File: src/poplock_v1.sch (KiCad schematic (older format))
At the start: 0 parts

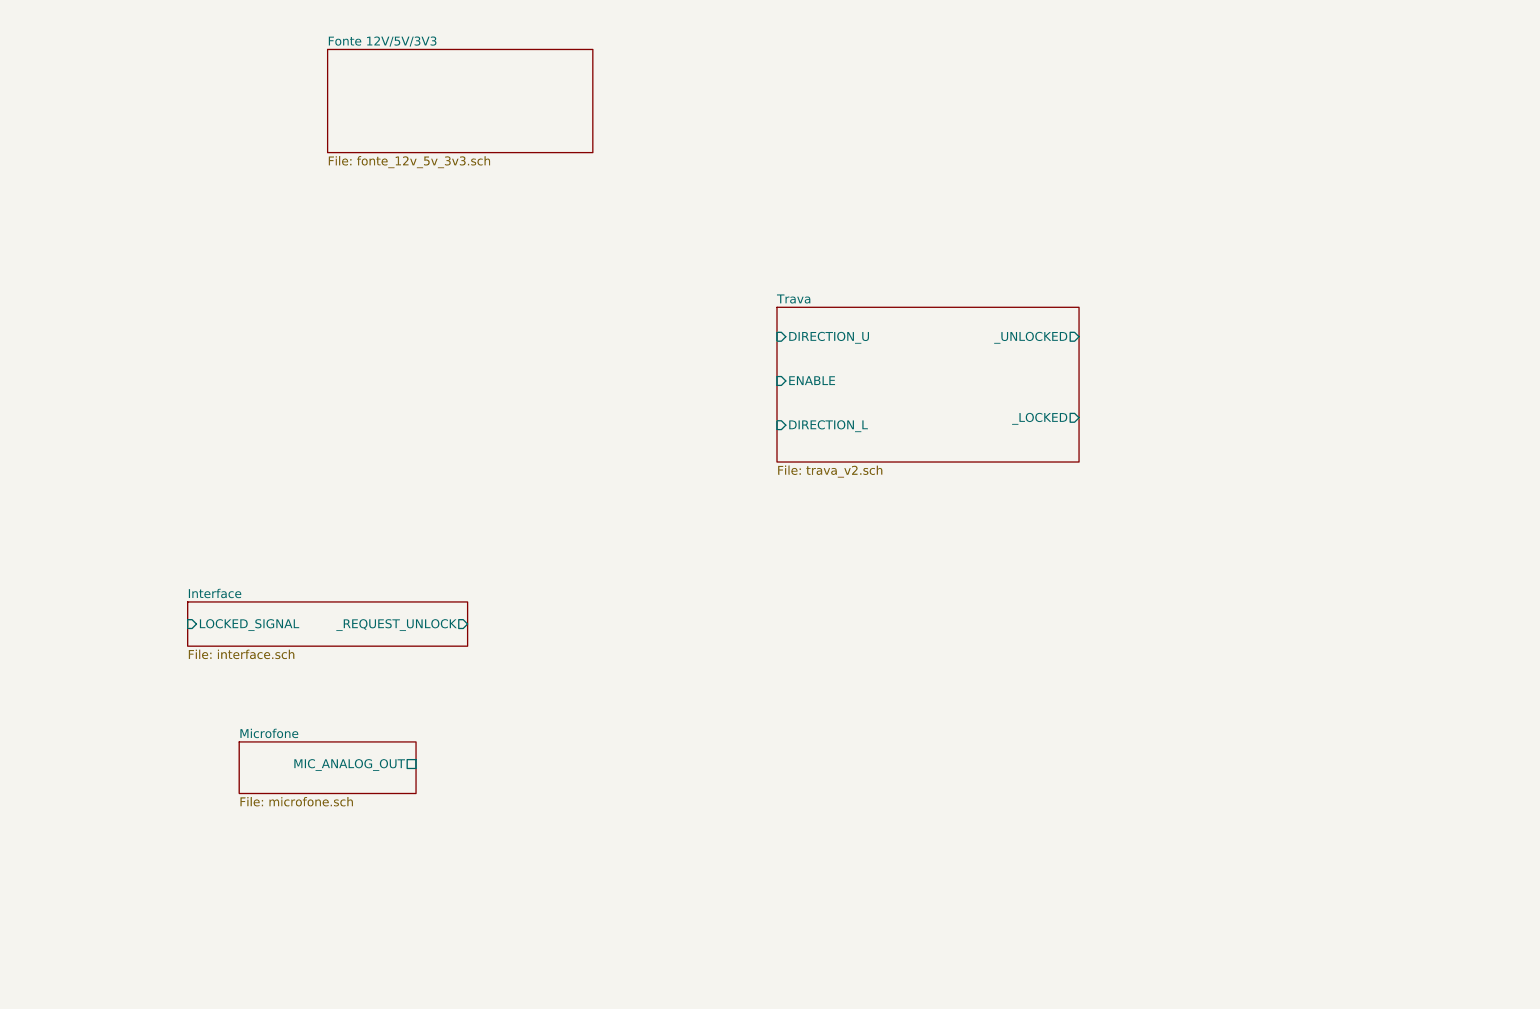
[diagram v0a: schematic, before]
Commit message: Adicionados conectores da FRDM-KL25Z e conexões básicas de alimentação
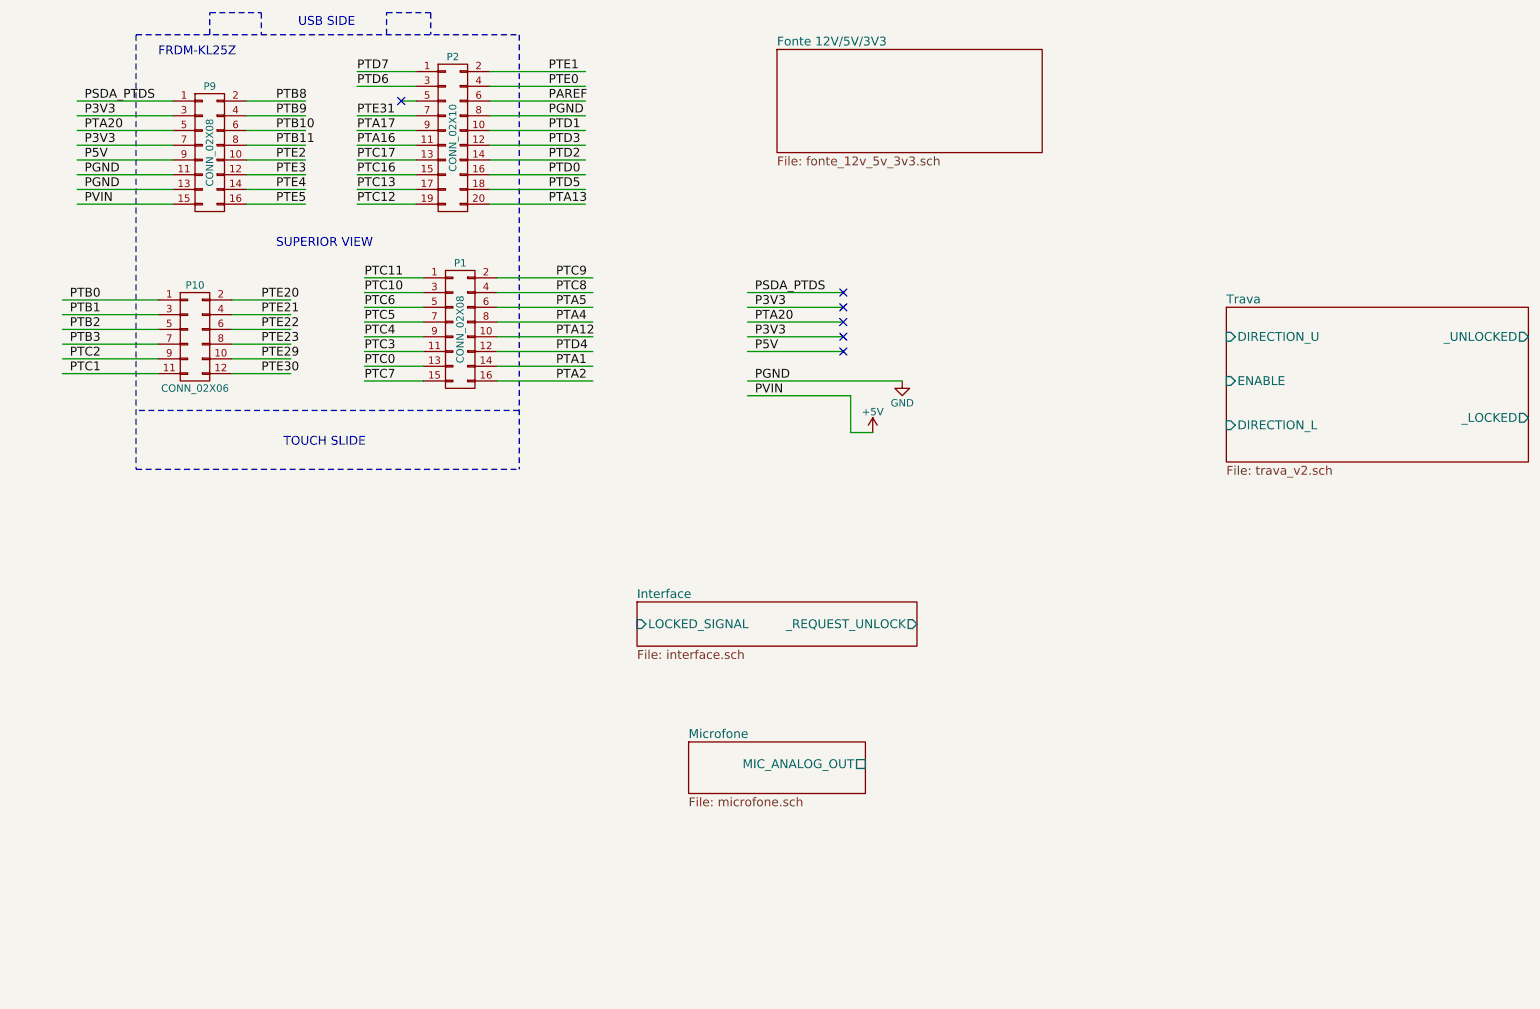
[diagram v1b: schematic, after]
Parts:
- added P1, P9: CONN_02X08, symbol CONN_02X08
- added P10: CONN_02X06, symbol CONN_02X06
- added P2: CONN_02X10, symbol CONN_02X10
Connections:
- net labels added: +5V, GND, P3V3, P5V, PAREF, PGND, PSDA_PTDS, PTA1, PTA12, PTA13, PTA16, PTA17, PTA2, PTA20, PTA4, PTA5, PTB0, PTB1, PTB10, PTB11, PTB2, PTB3, PTB8, PTB9, PTC0, PTC1, PTC10, PTC11, PTC12, PTC13, PTC16, PTC17, PTC2, PTC3, PTC4, PTC5, PTC6, PTC7, PTC8, PTC9, PTD0, PTD1, PTD2, PTD3, PTD4, PTD5, PTD6, PTD7, PTE0, PTE1, PTE2, PTE20, PTE21, PTE22, PTE23, PTE29, PTE3, PTE30, PTE31, PTE4, PTE5, PVIN
- wire segments 0 -> 73
- no-connect marks 0 -> 6
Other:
- note added: "FRDM-KL25Z"
- note added: "SUPERIOR VIEW"
- note added: "TOUCH SLIDE"
- note added: "USB SIDE"

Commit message: Acréscimo de bibliotecas de símbolo e de footprint do ESP12E retiradas de https://github.com/jdunmire/kicad-ESP8266 . As conexões necessárias com a KL25Z também foram realizadas.
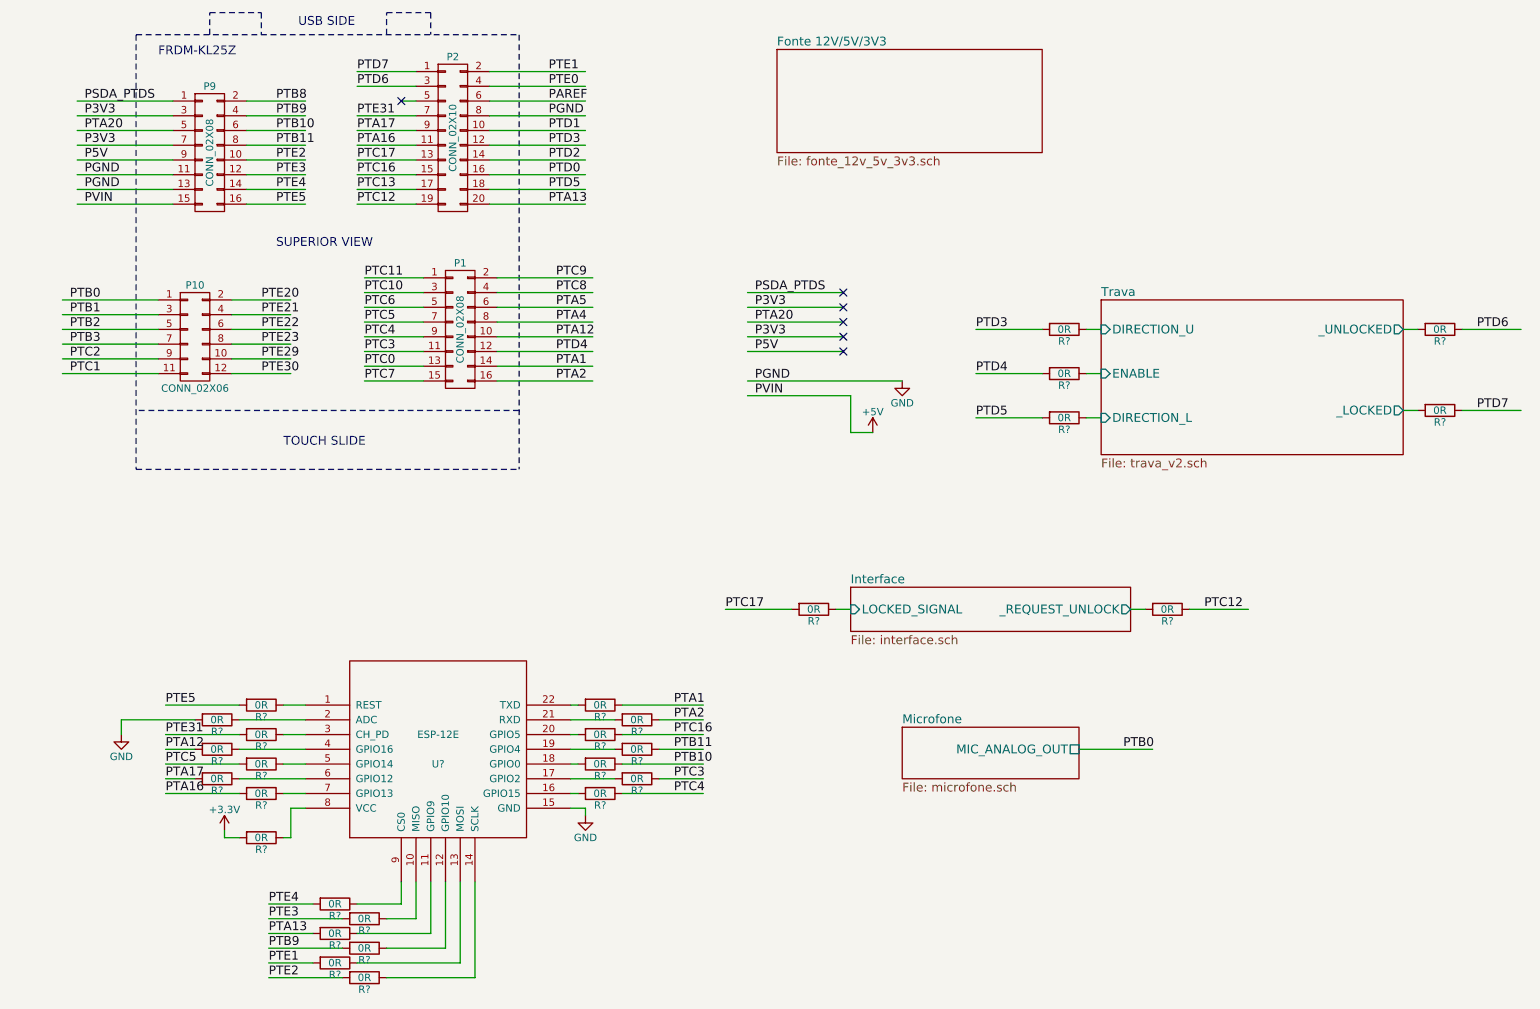
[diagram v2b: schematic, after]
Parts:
- added R? (x28): 0R, symbol R
- added U?: ESP-12E, symbol ESP-12E
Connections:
- net labels added: +3.3V
- wire segments 73 -> 142

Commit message: Verificação ERC -- checagem de erros elétricos no esquema -- concluída com sucesso. Há apenas dois warnings que não indicam problemas.
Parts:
- P1, P9: footprint (none) -> Pin_Headers:Pin_Header_Straight_2x08
- P10: footprint (none) -> Pin_Headers:Pin_Header_Straight_2x06
- P2: footprint (none) -> Pin_Headers:Pin_Header_Straight_2x10
- R23: renamed from R?; footprint (none) -> SMD_Packages:SMD-1210_Pol
- gave numbers to parts that had none: 28
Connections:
- net labels added: P3V3_2
- wire segments 142 -> 136
- no-connect marks 6 -> 33

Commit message: Footprint atualizado
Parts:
- R1, R10, R11, R12, R13, R14, R15, R16, R17, R18, R19, R2, R20, R21, R22, R24, R25, R26, R27, R28, R3, R4, R5, R6, R7, R8, R9: footprint (none) -> Resistors_SMD:R_0603_HandSoldering
- R23: footprint SMD_Packages:SMD-1210_Pol -> Resistors_SMD:R_0603_HandSoldering
- U1: footprint (none) -> lib:ESP-12E
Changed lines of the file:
@@
 F 0 "U1" H 3500 5450 50  0000 C CNN
 F 1 "ESP-12E" H 3500 5650 50  0000 C CNN
-F 2 "" H 3500 5550 50  0001 C CNN
+F 2 "lib:ESP-12E" H 3500 5550 50  0001 C CNN
 F 3 "" H 3500 5550 50  0001 C CNN
 	1    3500 5550
@@
 F 0 "R4" V 2380 5250 50  0000 C CNN
 F 1 "0R" V 2300 5250 50  0000 C CNN
-F 2 "" V 2230 5250 50  0001 C CNN
+F 2 "Resistors_SMD:R_0603_HandSoldering" V 2230 5250 50  0001 C CNN
 F 3 "" H 2300 5250 50  0000 C CNN
 	1    2300 5250
@@
 F 0 "R1" V 2080 5350 50  0000 C CNN
 F 1 "0R" V 2000 5350 50  0000 C CNN
-F 2 "" V 1930 5350 50  0001 C CNN
+F 2 "Resistors_SMD:R_0603_HandSoldering" V 1930 5350 50  0001 C CNN
 F 3 "" H 2000 5350 50  0000 C CNN
 	1    2000 5350
@@
 F 0 "R5" V 2380 5450 50  0000 C CNN
 F 1 "0R" V 2300 5450 50  0000 C CNN
-F 2 "" V 2230 5450 50  0001 C CNN
+F 2 "Resistors_SMD:R_0603_HandSoldering" V 2230 5450 50  0001 C CNN
 F 3 "" H 2300 5450 50  0000 C CNN
 	1    2300 5450
@@
 F 0 "R2" V 2080 5550 50  0000 C CNN
 F 1 "0R" V 2000 5550 50  0000 C CNN
-F 2 "" V 1930 5550 50  0001 C CNN
+F 2 "Resistors_SMD:R_0603_HandSoldering" V 1930 5550 50  0001 C CNN
 F 3 "" H 2000 5550 50  0000 C CNN
 	1    2000 5550
@@
 F 0 "R6" V 2380 5650 50  0000 C CNN
 F 1 "0R" V 2300 5650 50  0000 C CNN
-F 2 "" V 2230 5650 50  0001 C CNN
+F 2 "Resistors_SMD:R_0603_HandSoldering" V 2230 5650 50  0001 C CNN
 F 3 "" H 2300 5650 50  0000 C CNN
 	1    2300 5650
@@
 F 0 "R3" V 2080 5750 50  0000 C CNN
 F 1 "0R" V 2000 5750 50  0000 C CNN
-F 2 "" V 1930 5750 50  0001 C CNN
+F 2 "Resistors_SMD:R_0603_HandSoldering" V 1930 5750 50  0001 C CNN
 F 3 "" H 2000 5750 50  0000 C CNN
 	1    2000 5750
@@
 F 0 "R7" V 2380 5850 50  0000 C CNN
 F 1 "0R" V 2300 5850 50  0000 C CNN
-F 2 "" V 2230 5850 50  0001 C CNN
+F 2 "Resistors_SMD:R_0603_HandSoldering" V 2230 5850 50  0001 C CNN
 F 3 "" H 2300 5850 50  0000 C CNN
 	1    2300 5850
@@
 F 0 "R8" V 2380 6150 50  0000 C CNN
 F 1 "0R" V 2300 6150 50  0000 C CNN
-F 2 "" V 2230 6150 50  0001 C CNN
+F 2 "Resistors_SMD:R_0603_HandSoldering" V 2230 6150 50  0001 C CNN
 F 3 "" H 2300 6150 50  0000 C CNN
 	1    2300 6150
@@
 F 0 "R18" V 4680 5850 50  0000 C CNN
 F 1 "0R" V 4600 5850 50  0000 C CNN
-F 2 "" V 4530 5850 50  0001 C CNN
+F 2 "Resistors_SMD:R_0603_HandSoldering" V 4530 5850 50  0001 C CNN
 F 3 "" H 4600 5850 50  0000 C CNN
 	1    4600 5850
@@
 F 0 "R21" V 4930 5750 50  0000 C CNN
 F 1 "0R" V 4850 5750 50  0000 C CNN
-F 2 "" V 4780 5750 50  0001 C CNN
+F 2 "Resistors_SMD:R_0603_HandSoldering" V 4780 5750 50  0001 C CNN
 F 3 "" H 4850 5750 50  0000 C CNN
 	1    4850 5750
@@
 F 0 "R17" V 4680 5650 50  0000 C CNN
 F 1 "0R" V 4600 5650 50  0000 C CNN
-F 2 "" V 4530 5650 50  0001 C CNN
+F 2 "Resistors_SMD:R_0603_HandSoldering" V 4530 5650 50  0001 C CNN
 F 3 "" H 4600 5650 50  0000 C CNN
 	1    4600 5650
@@
 F 0 "R20" V 4930 5550 50  0000 C CNN
 F 1 "0R" V 4850 5550 50  0000 C CNN
-F 2 "" V 4780 5550 50  0001 C CNN
+F 2 "Resistors_SMD:R_0603_HandSoldering" V 4780 5550 50  0001 C CNN
 F 3 "" H 4850 5550 50  0000 C CNN
 	1    4850 5550
@@
 F 0 "R16" V 4680 5450 50  0000 C CNN
 F 1 "0R" V 4600 5450 50  0000 C CNN
-F 2 "" V 4530 5450 50  0001 C CNN
+F 2 "Resistors_SMD:R_0603_HandSoldering" V 4530 5450 50  0001 C CNN
 F 3 "" H 4600 5450 50  0000 C CNN
 	1    4600 5450
@@
 F 0 "R19" V 4930 5350 50  0000 C CNN
 F 1 "0R" V 4850 5350 50  0000 C CNN
-F 2 "" V 4780 5350 50  0001 C CNN
+F 2 "Resistors_SMD:R_0603_HandSoldering" V 4780 5350 50  0001 C CNN
 F 3 "" H 4850 5350 50  0000 C CNN
 	1    4850 5350
@@
 F 0 "R15" V 4680 5250 50  0000 C CNN
 F 1 "0R" V 4600 5250 50  0000 C CNN
-F 2 "" V 4530 5250 50  0001 C CNN
+F 2 "Resistors_SMD:R_0603_HandSoldering" V 4530 5250 50  0001 C CNN
 F 3 "" H 4600 5250 50  0000 C CNN
 	1    4600 5250
@@
 F 0 "R9" V 2880 6600 50  0000 C CNN
 F 1 "0R" V 2800 6600 50  0000 C CNN
-F 2 "" V 2730 6600 50  0001 C CNN
+F 2 "Resistors_SMD:R_0603_HandSoldering" V 2730 6600 50  0001 C CNN
 F 3 "" H 2800 6600 50  0000 C CNN
 	1    2800 6600
@@
 F 0 "R12" V 3080 6700 50  0000 C CNN
 F 1 "0R" V 3000 6700 50  0000 C CNN
-F 2 "" V 2930 6700 50  0001 C CNN
+F 2 "Resistors_SMD:R_0603_HandSoldering" V 2930 6700 50  0001 C CNN
 F 3 "" H 3000 6700 50  0000 C CNN
 	1    3000 6700
@@
 F 0 "R10" V 2880 6800 50  0000 C CNN
 F 1 "0R" V 2800 6800 50  0000 C CNN
-F 2 "" V 2730 6800 50  0001 C CNN
+F 2 "Resistors_SMD:R_0603_HandSoldering" V 2730 6800 50  0001 C CNN
 F 3 "" H 2800 6800 50  0000 C CNN
 	1    2800 6800
@@
 F 0 "R13" V 3080 6900 50  0000 C CNN
 F 1 "0R" V 3000 6900 50  0000 C CNN
-F 2 "" V 2930 6900 50  0001 C CNN
+F 2 "Resistors_SMD:R_0603_HandSoldering" V 2930 6900 50  0001 C CNN
 F 3 "" H 3000 6900 50  0000 C CNN
 	1    3000 6900
@@
 F 0 "R11" V 2880 7000 50  0000 C CNN
 F 1 "0R" V 2800 7000 50  0000 C CNN
-F 2 "" V 2730 7000 50  0001 C CNN
+F 2 "Resistors_SMD:R_0603_HandSoldering" V 2730 7000 50  0001 C CNN
 F 3 "" H 2800 7000 50  0000 C CNN
 	1    2800 7000
@@
 F 0 "R14" V 3080 7100 50  0000 C CNN
 F 1 "0R" V 3000 7100 50  0000 C CNN
-F 2 "" V 2930 7100 50  0001 C CNN
+F 2 "Resistors_SMD:R_0603_HandSoldering" V 2930 7100 50  0001 C CNN
 F 3 "" H 3000 7100 50  0000 C CNN
 	1    3000 7100
@@
 F 0 "R22" V 6130 4600 50  0000 C CNN
 F 1 "0R" V 6050 4600 50  0000 C CNN
-F 2 "" V 5980 4600 50  0001 C CNN
+F 2 "Resistors_SMD:R_0603_HandSoldering" V 5980 4600 50  0001 C CNN
 F 3 "" H 6050 4600 50  0000 C CNN
 	1    6050 4600
@@
 F 0 "R26" V 8530 4600 50  0000 C CNN
 F 1 "0R" V 8450 4600 50  0000 C CNN
-F 2 "" V 8380 4600 50  0001 C CNN
+F 2 "Resistors_SMD:R_0603_HandSoldering" V 8380 4600 50  0001 C CNN
 F 3 "" H 8450 4600 50  0000 C CNN
 	1    8450 4600
@@
 F 0 "R27" V 10380 2700 50  0000 C CNN
 F 1 "0R" V 10300 2700 50  0000 C CNN
-F 2 "" V 10230 2700 50  0001 C CNN
+F 2 "Resistors_SMD:R_0603_HandSoldering" V 10230 2700 50  0001 C CNN
 F 3 "" H 10300 2700 50  0000 C CNN
 	1    10300 2700
@@
 F 0 "R28" V 10380 3250 50  0000 C CNN
 F 1 "0R" V 10300 3250 50  0000 C CNN
-F 2 "" V 10230 3250 50  0001 C CNN
+F 2 "Resistors_SMD:R_0603_HandSoldering" V 10230 3250 50  0001 C CNN
 F 3 "" H 10300 3250 50  0000 C CNN
 	1    10300 3250
@@
 F 0 "R23" V 7830 2700 50  0000 C CNN
 F 1 "0R" V 7750 2700 50  0000 C CNN
-F 2 "SMD_Packages:SMD-1210_Pol" V 7500 2450 50  0001 C CNN
+F 2 "Resistors_SMD:R_0603_HandSoldering" V 7500 2450 50  0001 C CNN
 F 3 "" H 7750 2700 50  0000 C CNN
 	1    7750 2700
@@
 F 0 "R24" V 7830 3000 50  0000 C CNN
 F 1 "0R" V 7750 3000 50  0000 C CNN
-F 2 "" V 7680 3000 50  0001 C CNN
+F 2 "Resistors_SMD:R_0603_HandSoldering" V 7680 3000 50  0001 C CNN
 F 3 "" H 7750 3000 50  0000 C CNN
 	1    7750 3000
@@
 F 0 "R25" V 7830 3300 50  0000 C CNN
 F 1 "0R" V 7750 3300 50  0000 C CNN
-F 2 "" V 7680 3300 50  0001 C CNN
+F 2 "Resistors_SMD:R_0603_HandSoldering" V 7680 3300 50  0001 C CNN
 F 3 "" H 7750 3300 50  0000 C CNN
 	1    7750 3300

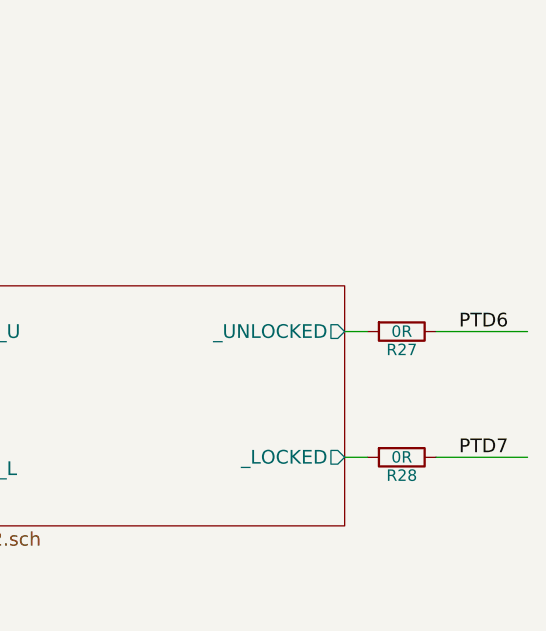
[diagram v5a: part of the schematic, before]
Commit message: PCB completa, feita a primeira revisão.
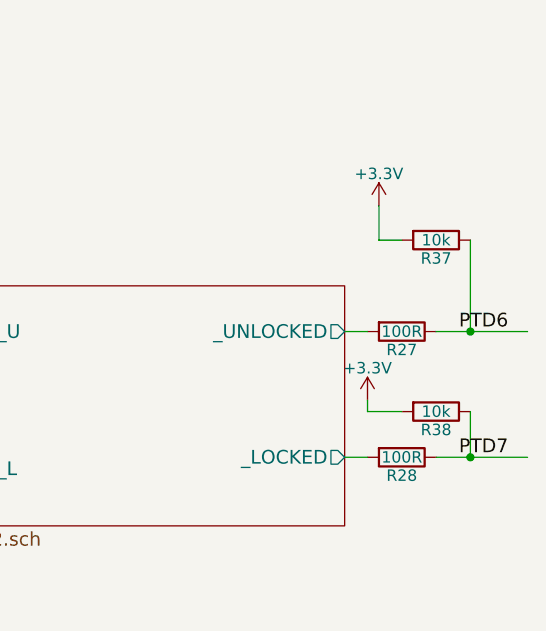
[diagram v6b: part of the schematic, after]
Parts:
- added R37, R38: 10k, Resistors_SMD:R_0603_HandSoldering, symbol R
- R27, R28: value 0R -> 100R
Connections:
- wire segments 136 -> 142
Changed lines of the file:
@@
 P 10300 2700
 F 0 "R27" V 10380 2700 50  0000 C CNN
-F 1 "0R" V 10300 2700 50  0000 C CNN
+F 1 "100R" V 10300 2700 50  0000 C CNN
 F 2 "Resistors_SMD:R_0603_HandSoldering" V 10230 2700 50  0001 C CNN
 F 3 "" H 10300 2700 50  0000 C CNN
@@
 P 10300 3250
 F 0 "R28" V 10380 3250 50  0000 C CNN
-F 1 "0R" V 10300 3250 50  0000 C CNN
+F 1 "100R" V 10300 3250 50  0000 C CNN
 F 2 "Resistors_SMD:R_0603_HandSoldering" V 10230 3250 50  0001 C CNN
 F 3 "" H 10300 3250 50  0000 C CNN
@@
 NoConn ~ 1050 1250
 NoConn ~ 1050 1150
+$Comp
+L R R37
+U 1 1 57E40E09
+P 10450 2300
+F 0 "R37" V 10530 2300 50  0000 C CNN
+F 1 "10k" V 10450 2300 50  0000 C CNN
+F 2 "Resistors_SMD:R_0603_HandSoldering" V 10380 2300 50  0001 C CNN
+F 3 "" H 10450 2300 50  0000 C CNN
+	1    10450 2300
+	0    1    1    0
+$EndComp
+$Comp
+L R R38
+U 1 1 57E40EFF
+P 10450 3050
+F 0 "R38" V 10530 3050 50  0000 C CNN
+F 1 "10k" V 10450 3050 50  0000 C CNN
+F 2 "Resistors_SMD:R_0603_HandSoldering" V 10380 3050 50  0001 C CNN
+F 3 "" H 10450 3050 50  0000 C CNN
+	1    10450 3050
+	0    1    1    0
+$EndComp
+$Comp
+L +3.3V #PWR06
+U 1 1 57E410ED
+P 10200 2150
+F 0 "#PWR06" H 10200 2000 50  0001 C CNN
+F 1 "+3.3V" H 10200 2290 50  0000 C CNN
+F 2 "" H 10200 2150 50  0000 C CNN
+F 3 "" H 10200 2150 50  0000 C CNN
+	1    10200 2150
+	1    0    0    -1
+$EndComp
+Wire Wire Line
+	10200 2150 10200 2300
+Wire Wire Line
+	10200 2300 10300 2300
+Wire Wire Line
+	10600 2300 10600 2700
+Connection ~ 10600 2700
+$Comp
+L +3.3V #PWR07
+U 1 1 57E42238
+P 10150 3000
+F 0 "#PWR07" H 10150 2850 50  0001 C CNN
+F 1 "+3.3V" H 10150 3140 50  0000 C CNN
+F 2 "" H 10150 3000 50  0000 C CNN
+F 3 "" H 10150 3000 50  0000 C CNN
+	1    10150 3000
+	1    0    0    -1
+$EndComp
+Wire Wire Line
+	10150 3000 10150 3050
+Wire Wire Line
+	10150 3050 10300 3050
+Wire Wire Line
+	10600 3050 10600 3250
+Connection ~ 10600 3250
 $EndSCHEMATC
